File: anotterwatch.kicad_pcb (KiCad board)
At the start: 2 copper layers, 48.5 x 43 mm, 82 parts, among them J1 USB_C_Receptacle_USB2.0, J2 Conn_01x05, Q1 Q_NMOS_GSD, Q2 nfet, Q3 npn, Q4 npn, Q5 2N7002, Q6 2N7002, U1 USBLC6-4SC6, U10 TS5A2053, U11 ADS7946SRTET, U2 ESP32, U3 CH340C, U4 ST7789V, U5 REF2915, U6 TCA9535MRGER, U7 TLV9062S, U8 OPA2322S, U9 TS5A2053

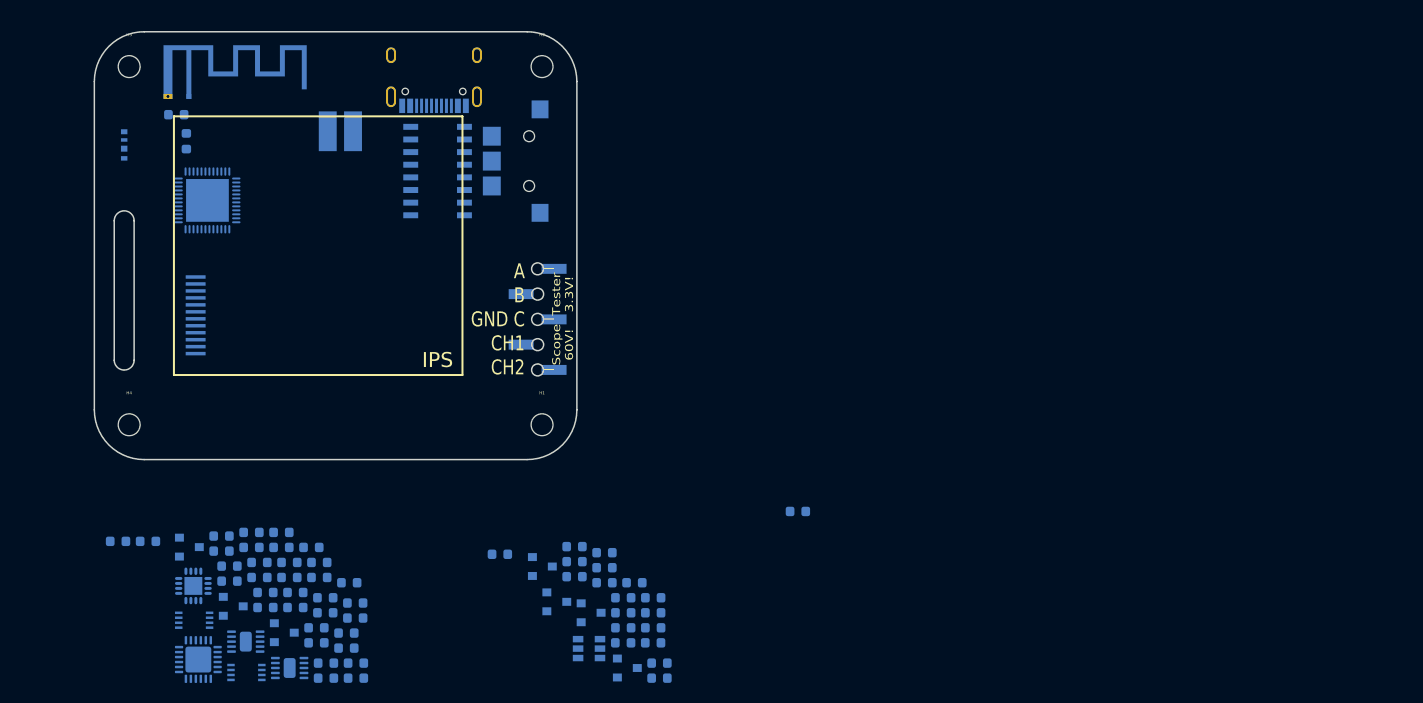
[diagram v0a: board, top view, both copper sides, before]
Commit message: added SD Card socket footprint
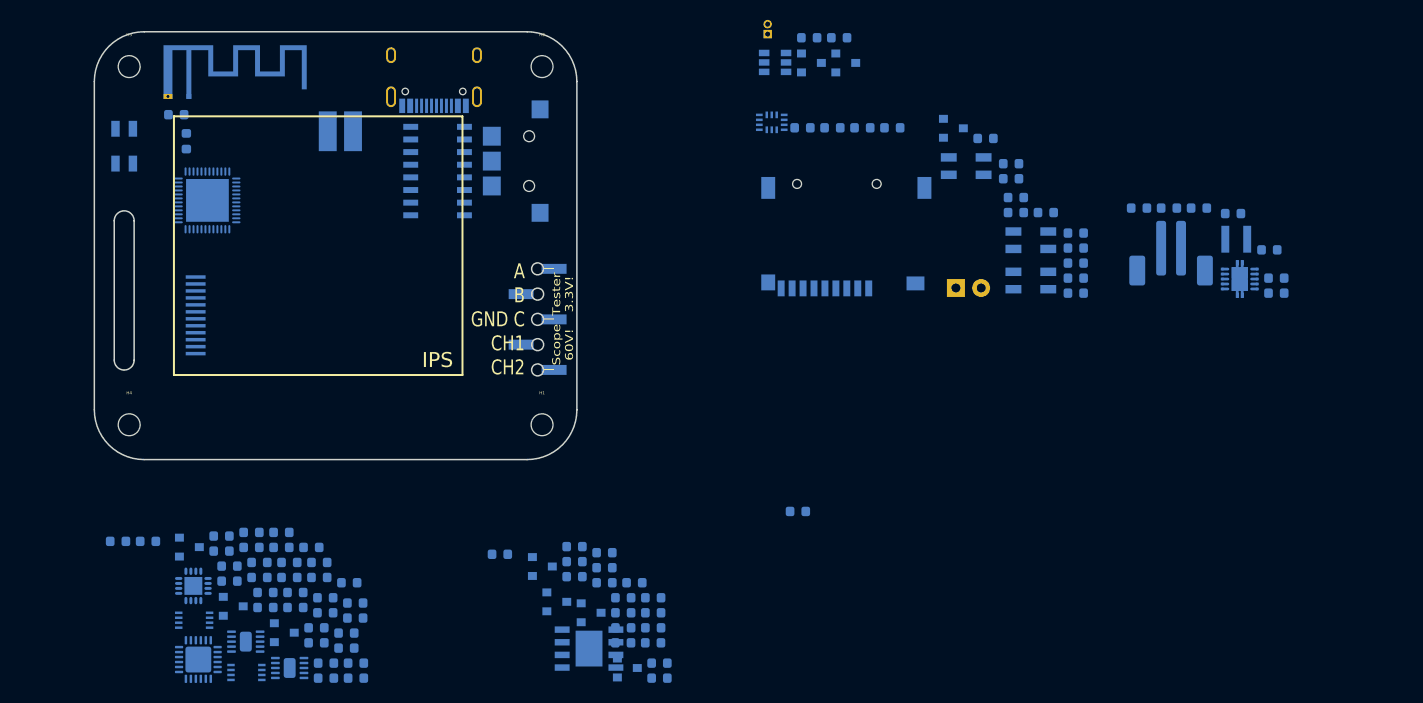
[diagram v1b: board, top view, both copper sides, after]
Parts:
- added C26: 100n, Capacitor_SMD:C_0603_1608Metric, B.Cu at (192.5, 86.8)
- added C27: 100n, Capacitor_SMD:C_0603_1608Metric, B.Cu at (186.0, 86.2)
- added C28: 100n, Capacitor_SMD:C_0603_1608Metric, B.Cu at (189.0, 86.2)
- added C29: 10u, Capacitor_SMD:C_0603_1608Metric, B.Cu at (196.8, 93.3)
- added C30: 100n, Capacitor_SMD:C_0603_1608Metric, B.Cu at (167.6, 79.2)
- added D2: LED, LED_THT:LED_D5.0mm_Horizontal_O1.27mm_Z9.0mm, B.Cu at (164.6, 94.3)
- added D4: SK6812MINI, LED_SMD:LED_SK6812MINI_PLCC4_3.5x3.5mm_P1.75mm, B.Cu at (172.1, 89.5)
- added D5: SK6812MINI, LED_SMD:LED_SK6812MINI_PLCC4_3.5x3.5mm_P1.75mm, B.Cu at (172.1, 93.5)
- added D6: SK6812MINI, LED_SMD:LED_SK6812MINI_PLCC4_3.5x3.5mm_P1.75mm, B.Cu at (165.6, 82.0)
- added FB1: Ferret, Inductor_SMD:L_0603_1608Metric, B.Cu at (152.9, 69.1)
- added J3: Micro_SD_Card, ST-TF-003A:SUNTECH_ST-TF-003A, B.Cu at (152.3, 89.0)
- added J4: Bat, Connector_JST:JST_PH_B2B-PH-SM4-TB_1x02-1MP_P2.00mm_Vertical, B.Cu at (186.2, 90.8)
- added L2: 2.2u, Inductor_SMD:L_Taiyo-Yuden_MD-3030, B.Cu at (192.8, 89.4)
- added LS1: Speaker, Connector_PinHeader_1.00mm:PinHeader_1x02_P1.00mm_Vertical, B.Cu at (145.7, 68.7)
- added Q7: AO3400, Package_TO_SOT_SMD:SOT-23, B.Cu at (164.3, 78.2)
- added Q8: 2N7002, Package_TO_SOT_SMD:SOT-23, B.Cu at (153.5, 71.6)
- added Q9: 2N7002, Package_TO_SOT_SMD:SOT-23, B.Cu at (150.1, 71.6)
- added R30: 10, Resistor_SMD:R_0603_1608Metric, B.Cu at (176.6, 90.2)
- added R31: 47k, Resistor_SMD:R_0603_1608Metric, B.Cu at (173.6, 86.7)
- added R32: 220, Resistor_SMD:R_0603_1608Metric, B.Cu at (170.1, 81.8)
- added R33: 47k, Resistor_SMD:R_0603_1608Metric, B.Cu at (176.6, 88.7)
- added R34: 47k, Resistor_SMD:R_0603_1608Metric, B.Cu at (170.6, 86.7)
- added R35: 10, Resistor_SMD:R_0603_1608Metric, B.Cu at (176.6, 91.8)
- added R36: 47k, Resistor_SMD:R_0603_1608Metric, B.Cu at (196.1, 90.4)
- added R37: 10, Resistor_SMD:R_0603_1608Metric, B.Cu at (170.6, 85.2)
- added R38: 5k1, Resistor_SMD:R_0603_1608Metric, B.Cu at (152.2, 78.2)
- added R39: 5k1, Resistor_SMD:R_0603_1608Metric, B.Cu at (176.6, 94.8)
- added R40: 47k, Resistor_SMD:R_0603_1608Metric, B.Cu at (176.6, 93.3)
- added R41: 47k, Resistor_SMD:R_0603_1608Metric, B.Cu at (158.2, 78.2)
- added R42: 5k1, Resistor_SMD:R_0603_1608Metric, B.Cu at (155.2, 78.2)
- added R43: 2k5, Resistor_SMD:R_0603_1608Metric, B.Cu at (183.0, 86.2)
- added R44: 47k, Resistor_SMD:R_0603_1608Metric, B.Cu at (149.2, 78.2)
- added R45: 47k, Resistor_SMD:R_0603_1608Metric, B.Cu at (170.1, 83.3)
- added R46: 47k, Resistor_SMD:R_0603_1608Metric, B.Cu at (149.9, 69.1)
- added R47: 100, Resistor_SMD:R_0603_1608Metric, B.Cu at (196.8, 94.8)
- added U12: BMI270, badgelib:BMI270, B.Cu at (146.1, 77.6)
- added U13: USBLC6-4SC6, Package_TO_SOT_SMD:SOT-23-6, B.Cu at (146.4, 71.6)
- added U14: TPS63001DRCR, Package_SON:Texas_S-PVSON-N10, B.Cu at (193.1, 93.4)
- C3: value 100n -> 10u
- C6: value 100n -> 4u7
- D1: value SK6812 -> SK6812MINI; footprint badgelib:sk6812_side -> LED_SMD:LED_SK6812MINI_PLCC4_3.5x3.5mm_P1.75mm
- Q1: value Q_NMOS_GSD -> AO3400
- Q2: value nfet -> AO3400
- R10, R9: value 100k -> 47k
- R3, R4, R6: value 10k -> 47k
- U1: value USBLC6-4SC6 -> TP4056; footprint Package_TO_SOT_SMD:SOT-23-6 -> Package_SO:Diodes_PSOP-8
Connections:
- net CH340_V3 renamed Net-(C4-Pad1)
- net Net-(U2-Pad5) renamed ESP_ADC
- C10 pad 1: VCC -> TPS_FB
- C13 pad 1: +3V3 -> TPS_FB
- C14 pad 1: +3V3 -> TPS_FB
- C15 pad 1: +3V3 -> TPS_FB
- C17 pad 1: +3V3 -> TPS_FB
- C19 pad 1: +3V3 -> TPS_FB
- C2 pad 1: VCC -> VBUS
- C24 pad 2: GNDA -> Net-(C24-Pad2)
- C25 pad 2: GNDA -> Net-(C25-Pad2)
- C3 pad 1: VCC -> +BATT
- C5 pad 1: VBUS -> IPS_RST
- C6 pad 1: VCC -> Net-(C6-Pad1)
- C6 pad 2: GND -> Net-(C6-Pad2)
- C7 pad 1: VCC -> Net-(C7-Pad1)
- C7 pad 2: GND -> GNDA
- C8 pad 1: VCC -> TPS_FB
- J1 pad A6: Dp -> USB_DP
- J1 pad A7: Dn -> USB_DN
- J1 pad B6: Dp -> USB_DP
- J1 pad B7: Dn -> USB_DN
- Q1 pad 1: White_LED -> WHITE_LED
- Q5 pad 3: Net-(Q5-Pad3) -> Net-(C24-Pad2)
- Q6 pad 3: Net-(Q6-Pad3) -> Net-(C25-Pad2)
- R10 pad 2: Net-(R10-Pad2) -> ESP32_DAC
- R12 pad 2: Net-(R12-Pad2) -> Net-(C6-Pad1)
- R28 pad 1: Net-(Q5-Pad3) -> Net-(C24-Pad2)
- R29 pad 1: Net-(Q6-Pad3) -> Net-(C25-Pad2)
- R3 pad 1: VCC -> TPS_FB
- R4 pad 1: White_LED -> WHITE_LED
- R6 pad 1: IPS_LED -> TPS_FB
- R6 pad 2: GND -> IO0
- R9 pad 1: Net-(R10-Pad2) -> ESP32_DAC
- S1 pad 1: Net-(S1-Pad1) -> BTN_UP
- S1 pad 2: Net-(S1-Pad2) -> BTN_DOWN
- S1 pad T: Net-(S1-PadT) -> BTN_CNTR
- U1 pad 1: Net-(U1-Pad1) -> GND
- U1 pad 2: GND -> Net-(R43-Pad1)
- U1 pad 3: Net-(U1-Pad3) -> GND
- U1 pad 4: Dp -> VBUS
- U1 pad 5: VCC -> +BATT
- U1 pad 6: Dn -> Net-(U1-Pad6)
- U10 pad 8: +3V3 -> TPS_FB
- U11 pad 11: Net-(U11-Pad11) -> ADC_CH_SEL
- U11 pad 12: Net-(U11-Pad12) -> ADC_ENABLE
- U11 pad 13: Net-(U11-Pad13) -> ADC_CS
- U11 pad 14: Net-(U11-Pad14) -> ADC_SCK
- U11 pad 15: Net-(U11-Pad15) -> ADC_MISO
- U11 pad 16: Net-(U11-Pad16) -> TPS_FB
- U11 pad 17: Net-(U11-Pad17) -> GND
- U11 pad 2: Net-(U11-Pad2) -> Net-(C7-Pad1)
- U2 pad 1: VCC -> TPS_FB
- U2 pad 10: Net-(U2-Pad10) -> BTN_CNTR
- U2 pad 11: Net-(U2-Pad11) -> WAKE1
- U2 pad 12: Net-(U2-Pad12) -> WHITE_LED
- U2 pad 13: Net-(U2-Pad13) -> IPS_LED
- U2 pad 14: Net-(U2-Pad14) -> ESP32_DAC
- U2 pad 15: Net-(U2-Pad15) -> IPS_DC
- U2 pad 16: Net-(U2-Pad16) -> ADC_CH_SEL
- U2 pad 17: Net-(U2-Pad17) -> SD_CLK
- U2 pad 18: Net-(U2-Pad18) -> SD_DATA2
- U2 pad 19: VCC -> TPS_FB
- U2 pad 20: Net-(U2-Pad20) -> SD_DATA3
- U2 pad 21: Net-(U2-Pad21) -> SD_CMD
- U2 pad 22: Net-(U2-Pad22) -> SD_DATA0
- U2 pad 24: Net-(U2-Pad24) -> SD_DATA1
- U2 pad 3: VCC -> TPS_FB
- U2 pad 34: Net-(U2-Pad34) -> ADC_CS
- U2 pad 36: Net-(U2-Pad36) -> IPS_MOSI
- U2 pad 37: VCC -> TPS_FB
- U2 pad 38: Net-(U2-Pad38) -> ADC_MISO
- U2 pad 39: Net-(U2-Pad39) -> I2C_SCL
- U2 pad 4: VCC -> TPS_FB
- U2 pad 42: Net-(U2-Pad42) -> I2C_SDA
- U2 pad 43: VCC -> TPS_FB
- U2 pad 46: VCC -> TPS_FB
- U2 pad 6: Net-(U2-Pad6) -> CHRG
- U2 pad 7: Net-(U2-Pad7) -> BTN_UP
- U2 pad 8: Net-(U2-Pad8) -> BTN_DOWN
- U3 pad 5: Dp -> USB_DP
- U3 pad 6: Dn -> USB_DN
- U4 pad 3: VCC -> TPS_FB
- U4 pad 4: VCC -> TPS_FB
- U4 pad 7: IPS_CD -> IPS_DC
- U4 pad 8: IPS_CS -> GND
- U4 pad 9: VCC -> ADC_SCK
- U6 pad 19: SCL -> I2C_SCL
- U6 pad 20: SDA -> I2C_SDA
- U6 pad 21: +3V3 -> TPS_FB
- U6 pad 7: Net-(U6-Pad7) -> PARTY_ENABLE
- U7 pad 1: Net-(R12-Pad2) -> Net-(C6-Pad1)
- U7 pad 10: +3V3 -> TPS_FB
- U7 pad 2: Net-(R12-Pad2) -> Net-(C6-Pad1)
- U7 pad 3: Net-(R10-Pad2) -> ESP32_DAC
- U8 pad 10: +3V3 -> TPS_FB
- U9 pad 8: +3V3 -> TPS_FB

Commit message: UPD: finalized schematic, started layout
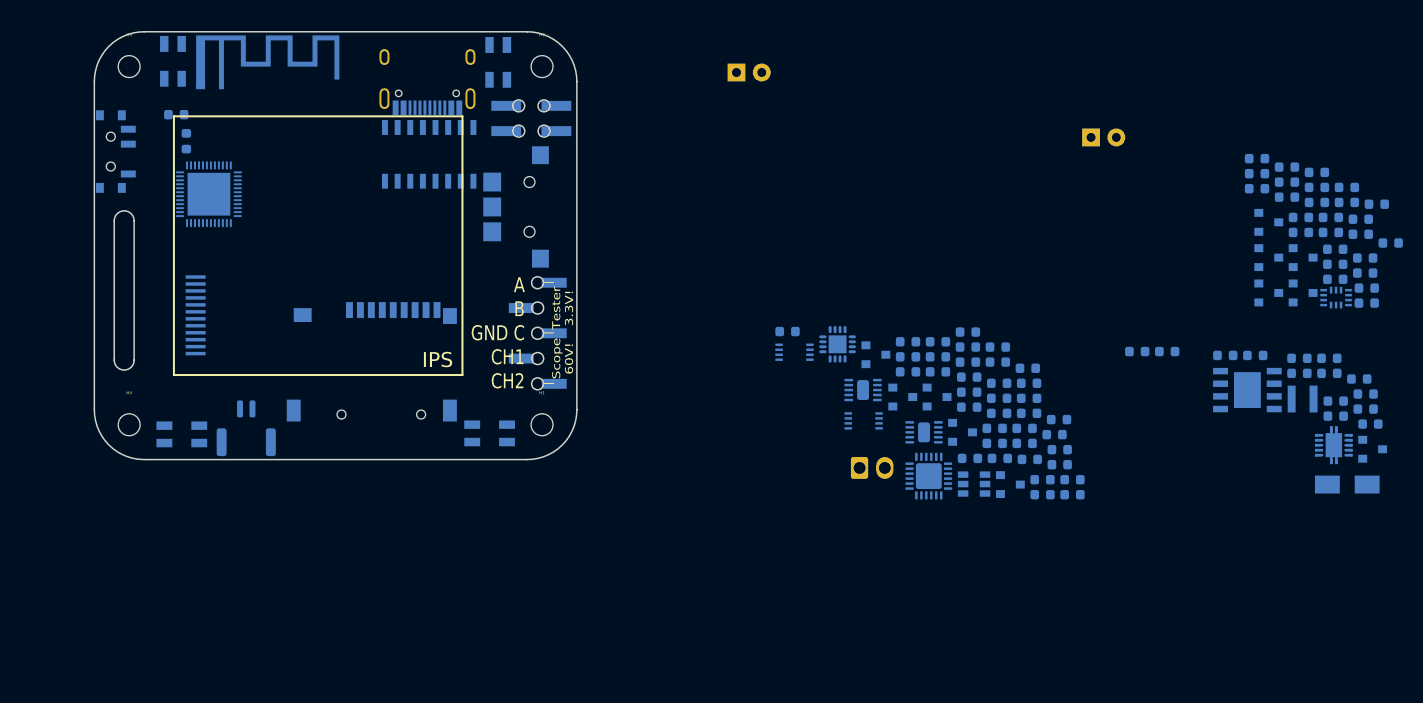
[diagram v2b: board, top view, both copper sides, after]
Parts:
- added BT1: 603020, Connector_JST:JST_GH_BM02B-GHS-TBT_1x02-1MP_P1.25mm_Vertical, B.Cu at (93.3, 108.4)
- added D7: D_Small, Diode_SMD:D_SMA, B.Cu at (203.9, 114.0)
- added Q10: Q_PMOS_GDS, Package_TO_SOT_SMD:SOT-23, B.Cu at (206.5, 110.5)
- added SW1: SW_SPST, Button_Switch_SMD:SW_SPDT_PCM12, B.Cu at (80.0, 80.5)
- C1: value 100p -> 100n
- C11, C12: value TBD -> 100n
- C15: value 100n -> 4u7
- C17, C18: value 100n -> 6n8
- C19: value 100n -> 1n
- C20: value 6n8 -> 1n
- C21: value 6n8 -> 33p
- C22: value 1n -> 33p
- C23: value 1n -> 100n
- C24: value 33p -> 100p
- C25: value 33p -> 10u
- C26, C27, C30: value 100n -> 10u
- C29, C8: value 10u -> 100n
- C6: value 4u7 -> TBD
- C7: value 100n -> TBD
- D2, D3: value LED -> SK6812MINI; footprint LED_THT:LED_D5.0mm_Horizontal_O1.27mm_Z9.0mm -> LED_SMD:LED_SK6812MINI_PLCC4_3.5x3.5mm_P1.75mm
- D5, D6: value SK6812MINI -> LED; footprint LED_SMD:LED_SK6812MINI_PLCC4_3.5x3.5mm_P1.75mm -> LED_THT:LED_D5.0mm_Horizontal_O1.27mm_Z9.0mm
- J1: value USB_C_Receptacle_USB2.0 -> Conn_02x02_Odd_Even; footprint badgelib:USB-C 16Pin -> Connector_PinSocket_2.54mm:PinSocket_2x02_P2.54mm_Vertical_SMD
- J2: value Conn_01x05 -> Micro_SD_Card; footprint Connector_PinHeader_2.54mm:PinHeader_1x05_P2.54mm_Vertical_SMD_Pin1Left -> ST-TF-003A:SUNTECH_ST-TF-003A
- J3: value Micro_SD_Card -> Conn_01x05; footprint ST-TF-003A:SUNTECH_ST-TF-003A -> Connector_PinHeader_2.54mm:PinHeader_1x05_P2.54mm_Vertical_SMD_Pin1Left
- J4: value Bat -> USB_C_Receptacle_USB2.0; footprint Connector_JST:JST_PH_B2B-PH-SM4-TB_1x02-1MP_P2.00mm_Vertical -> badgelib:USB-C 16Pin
- LS1: footprint Connector_PinHeader_1.00mm:PinHeader_1x02_P1.00mm_Vertical -> Connector_Molex:Molex_KK-254_AE-6410-02A_1x02_P2.54mm_Vertical
- Q3, Q4: value npn -> AO3400
- Q5: value 2N7002 -> AO3400
- Q7: value AO3400 -> 2N7002
- R11, R18: value 680 -> 10
- R13, R15: value 390k -> 10
- R14: value 680 -> 47k
- R16, R17: value 390k -> 47k
- R19, R20: value 10M -> 47k
- R21, R28: value 10M -> 680
- R22: value 10M -> 100
- R24: value 390k -> 680
- R26, R27: value 2M2 -> 390k
- R30: value 10 -> 10M
- R31, R40: value 47k -> 10M
- R32: value 220 -> 10M
- R33, R34: value 47k -> 390k
- R35: value 10 -> 390k
- R37: value 10 -> 2M2
- R38: value 5k1 -> 2M2
- R39: value 5k1 -> 10M
- R41, R44, R45, R9: value 47k -> 5k1
- R43: value 2k5 -> 390k
- R5: value 10 -> 47k
- R7, R8: value 10k -> 47k
- U1: value TP4056 -> BMI270; footprint Package_SO:Diodes_PSOP-8 -> badgelib:BMI270
- U11: value ADS7946SRTET -> TS5A2053; footprint Package_DFN_QFN:QFN-16-1EP_3x3mm_P0.5mm_EP1.8x1.8mm -> Package_SO:VSSOP-8_2.4x2.1mm_P0.5mm
- U12: value BMI270 -> ADS7946SRTET; footprint badgelib:BMI270 -> Package_DFN_QFN:QFN-16-1EP_3x3mm_P0.5mm_EP1.8x1.8mm
- U13: value USBLC6-4SC6 -> TP4056; footprint Package_TO_SOT_SMD:SOT-23-6 -> Package_SO:Diodes_PSOP-8
- U2: value ESP32 -> CH340C; footprint ESP32-footprints-Lib:ESP32 -> Package_SO:SOIC-16_3.9x9.9mm_P1.27mm
- U3: value CH340C -> ESP32; footprint Package_SO:SOIC-16_3.9x9.9mm_P1.27mm -> ESP32-footprints-Lib:ESP32
- U9: value TS5A2053 -> USBLC6-4SC6; footprint Package_SO:VSSOP-8_2.4x2.1mm_P0.5mm -> Package_TO_SOT_SMD:SOT-23-6
- moved R15 121.2 mm to (208.3, 89.7)
- moved R12 120.3 mm to (194.9, 82.8)
- moved R11 120.0 mm to (197.9, 83.6)
- moved R14 119.1 mm to (203.9, 84.1)
- moved R17 116.8 mm to (205.3, 87.3)
- moved R16 111.1 mm to (200.9, 82.6)
- moved Q5 111.0 mm to (196.0, 87.7)
- moved R13 110.5 mm to (202.3, 88.7)
- moved R10 109.8 mm to (205.7, 91.2)
- moved R18 107.5 mm to (203.9, 85.7)
- moved R9 104.5 mm to (200.9, 85.7)
- moved C24 103.6 mm to (199.1, 102.8)
- moved C25 103.0 mm to (202.1, 101.3)
- moved C8 88.4 mm to (202.7, 93.4)
- moved D4 87.5 mm to (86.8, 109.0), turned to 180 degrees
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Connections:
- C1 pad 1: Net-(C1-Pad1) -> VBUS
- C10 pad 1: TPS_FB -> +3V3
- C11 pad 1: Net-(C11-Pad1) -> +3V3
- C12 pad 1: Net-(AE1-Pad1) -> AFE_ENABLE
- C12 pad 2: GND -> GNDA
- C13 pad 1: TPS_FB -> +3V3
- C14 pad 1: TPS_FB -> ADC_REF
- C14 pad 2: GND -> GNDA
- C15 pad 1: TPS_FB -> Net-(C15-Pad1)
- C15 pad 2: GND -> Net-(C15-Pad2)
- C16 pad 1: AFE_ENABLE -> +3V3
- C16 pad 2: GNDA -> GND
- C17 pad 1: TPS_FB -> Net-(C17-Pad1)
- C17 pad 2: GND -> GNDA
- C18 pad 1: ADC_REF -> Net-(C18-Pad1)
- C19 pad 1: TPS_FB -> Net-(C19-Pad1)
- C19 pad 2: GND -> PROBE1
- C2 pad 1: VBUS -> Net-(C2-Pad1)
- C20 pad 2: GNDA -> PROBE2
- C21 pad 1: Net-(C21-Pad1) -> PROBE1
- C21 pad 2: GNDA -> Net-(C21-Pad2)
- C22 pad 1: Net-(C22-Pad1) -> PROBE2
- C22 pad 2: PROBE1 -> Net-(C22-Pad2)
- C23 pad 2: PROBE2 -> GNDA
- C24 pad 1: PROBE1 -> GND
- C25 pad 1: PROBE2 -> VBUS
- C25 pad 2: Net-(C25-Pad2) -> GND
- C26 pad 1: Net-(C26-Pad1) -> Net-(BT1-Pad1)
- C28 pad 1: TPS_FB -> Net-(C28-Pad1)
- C29 pad 1: TPS_FB -> +3V3
- C3 pad 1: +BATT -> +3V3
- C30 pad 1: VBUS -> +3V3
- C4 pad 1: Net-(C4-Pad1) -> EN
- C5 pad 1: IPS_RST -> +3V3
- C6 pad 2: Net-(C6-Pad2) -> GND
- C7 pad 1: Net-(C7-Pad1) -> Net-(AE1-Pad1)
- C7 pad 2: GNDA -> GND
- C8 pad 1: TPS_FB -> IPS_RST
- C9 pad 1: EN -> +3V3
- D1 pad 4: TPS_FB -> +3V3
- D2 pad 2: Net-(D2-Pad2) -> Net-(D1-Pad2)
- D3 pad 1: Net-(D2-Pad1) -> Net-(D3-Pad1)
- D3 pad 2: Net-(D3-Pad2) -> Net-(D1-Pad2)
- D4 pad 3: Net-(D1-Pad1) -> Net-(D3-Pad1)
- D4 pad 4: TPS_FB -> +3V3
- D5 pad 2: Net-(D1-Pad2) -> Net-(D5-Pad2)
- D6 pad 1: Net-(D6-Pad1) -> Net-(D5-Pad1)
- D6 pad 2: Net-(D1-Pad2) -> Net-(D6-Pad2)
- FB1 pad 1: Net-(C7-Pad1) -> Net-(C23-Pad1)
- FB1 pad 2: TPS_FB -> +3V3
- J2 pad 1: Net-(J2-Pad1) -> SD_DATA2
- J2 pad 2: Net-(J2-Pad2) -> SD_DATA3
- J2 pad 3: Net-(J2-Pad3) -> SD_CMD
- J2 pad 4: Net-(J2-Pad4) -> +3V3
- J3 pad 1: SD_DATA2 -> Net-(J3-Pad1)
- J3 pad 2: SD_DATA3 -> Net-(J3-Pad2)
- J3 pad 3: SD_CMD -> Net-(J3-Pad3)
- J3 pad 4: TPS_FB -> Net-(J3-Pad4)
- L1 pad 1: Net-(C11-Pad1) -> Net-(C6-Pad1)
- LS1 pad 1: Net-(C6-Pad2) -> Net-(C15-Pad2)
- Q1 pad 1: WHITE_LED -> DTR
- Q1 pad 2: GND -> RTS
- Q1 pad 3: Net-(D2-Pad1) -> EN
- Q2 pad 1: IPS_LED -> RTS
- Q2 pad 2: GND -> DTR
- Q2 pad 3: Net-(Q2-Pad3) -> IO0
- Q3 pad 1: Net-(Q3-Pad1) -> PARTY_ENABLE
- Q3 pad 2: Net-(Q3-Pad2) -> GND
- Q3 pad 3: EN -> Net-(D1-Pad2)
- Q4 pad 1: Net-(Q3-Pad2) -> IPS_LED
- Q4 pad 2: Net-(Q3-Pad1) -> GND
- Q4 pad 3: IO0 -> Net-(Q4-Pad3)
- Q5 pad 1: SE_ENABLE -> WHITE_LED
- Q5 pad 2: GNDA -> GND
- Q5 pad 3: Net-(C24-Pad2) -> Net-(D5-Pad1)
- Q6 pad 1: SE_ENABLE -> BUF_ENABLE
- Q6 pad 2: GNDA -> GND
- Q6 pad 3: Net-(C25-Pad2) -> Net-(LS1-Pad2)
- Q7 pad 1: PARTY_ENABLE -> AFE_ENABLE
- Q7 pad 3: Net-(D1-Pad2) -> ADC_ENABLE
- Q8 pad 1: AFE_ENABLE -> SE_ENABLE
- Q8 pad 2: GND -> GNDA
- Q8 pad 3: ADC_ENABLE -> Net-(C21-Pad2)
- Q9 pad 1: BUF_ENABLE -> SE_ENABLE
- Q9 pad 2: GND -> GNDA
- Q9 pad 3: Net-(LS1-Pad2) -> Net-(C22-Pad2)
- R1 pad 1: GND -> I2C_SDA
- R1 pad 2: Net-(J1-PadA5) -> +3V3
- R10 pad 1: GNDA -> +3V3
- R10 pad 2: ESP32_DAC -> BTN_CNTR
- R11 pad 1: Net-(J2-Pad3) -> Net-(J2-Pad5)
- R11 pad 2: Net-(R11-Pad2) -> SD_CLK
- R12 pad 1: Net-(J2-Pad3) -> Net-(J2-Pad7)
- R12 pad 2: Net-(C6-Pad1) -> SD_DATA0
- R13 pad 1: Net-(J2-Pad3) -> ADC_SCK
- R14 pad 1: Net-(J2-Pad2) -> PARTY_ENABLE
- R14 pad 2: Net-(R14-Pad2) -> GND
- R15 pad 1: Net-(J2-Pad2) -> +BATT
- R15 pad 2: Net-(R15-Pad2) -> Net-(D5-Pad2)
- R16 pad 1: Net-(C20-Pad1) -> WHITE_LED
- R16 pad 2: ADC_REF -> GND
- R17 pad 1: Net-(C21-Pad1) -> +3V3
- R17 pad 2: ADC_REF -> IPS_RST
- R18 pad 1: Net-(J2-Pad1) -> +BATT
- R18 pad 2: Net-(R18-Pad2) -> Net-(D6-Pad2)
- R19 pad 1: Net-(J2-Pad1) -> ESP32_DAC
- R19 pad 2: PROBE1 -> ADC_REF
- R2 pad 1: GND -> +3V3
- R2 pad 2: Net-(J1-PadB5) -> I2C_SCL
- R20 pad 1: Net-(J2-Pad2) -> GNDA
- R20 pad 2: PROBE2 -> ESP32_DAC
- R21 pad 1: Net-(J2-Pad4) -> Net-(J3-Pad3)
- R21 pad 2: PROBE1 -> Net-(R21-Pad2)
- R22 pad 1: Net-(J2-Pad5) -> Net-(J3-Pad3)
- R22 pad 2: PROBE2 -> Net-(C15-Pad1)
- R23 pad 1: GNDA -> Net-(J3-Pad3)
- R23 pad 2: Net-(C20-Pad1) -> Net-(R23-Pad2)
- R24 pad 1: GNDA -> Net-(J3-Pad2)
- R24 pad 2: Net-(C21-Pad1) -> Net-(R24-Pad2)
- R25 pad 1: Net-(J2-Pad1) -> Net-(J3-Pad2)
- R26 pad 1: PROBE1 -> Net-(C17-Pad1)
- R26 pad 2: Net-(C22-Pad1) -> ADC_REF
- R27 pad 1: PROBE2 -> Net-(C18-Pad1)
- R27 pad 2: Net-(C23-Pad1) -> ADC_REF
- R28 pad 1: Net-(C24-Pad2) -> Net-(J3-Pad1)
- R28 pad 2: PROBE1 -> Net-(R28-Pad2)
- R29 pad 1: Net-(C25-Pad2) -> Net-(J3-Pad1)
- R29 pad 2: PROBE2 -> PROBE1
- R3 pad 1: TPS_FB -> +3V3
- R3 pad 2: EN -> SD_DATA0
- R30 pad 1: Net-(J3-Pad5) -> Net-(J3-Pad2)
- R30 pad 2: SD_CLK -> PROBE2
- R31 pad 1: TPS_FB -> Net-(J3-Pad4)
- R31 pad 2: BTN_UP -> PROBE1
- R32 pad 1: Net-(J3-Pad7) -> Net-(J3-Pad5)
- R32 pad 2: SD_DATA0 -> PROBE2
- R33 pad 1: TPS_FB -> GNDA
- R33 pad 2: BTN_DOWN -> Net-(C17-Pad1)
- R34 pad 1: TPS_FB -> GNDA
- R34 pad 2: BTN_CNTR -> Net-(C18-Pad1)
- R35 pad 1: ADC_SCK -> Net-(J3-Pad1)
- R36 pad 1: TPS_FB -> ADC_ENABLE
- R36 pad 2: CHRG -> +3V3
- R37 pad 1: +BATT -> PROBE1
- R37 pad 2: Net-(D2-Pad2) -> Net-(C19-Pad1)
- R38 pad 1: I2C_SDA -> PROBE2
- R38 pad 2: TPS_FB -> Net-(C20-Pad1)
- R39 pad 1: TPS_FB -> Net-(C21-Pad2)
- R39 pad 2: I2C_SCL -> PROBE1
- R4 pad 1: WHITE_LED -> +3V3
- R4 pad 2: GND -> IO0
- R40 pad 1: TPS_FB -> Net-(C22-Pad2)
- R40 pad 2: SD_DATA0 -> PROBE2
- R41 pad 1: TPS_FB -> GND
- R41 pad 2: SD_DATA3 -> Net-(J4-PadA5)
- R42 pad 1: TPS_FB -> GND
- R42 pad 2: SD_CMD -> Net-(J4-PadB5)
- R43 pad 1: Net-(R43-Pad1) -> +3V3
- R43 pad 2: GND -> CHRG
- R44 pad 1: PARTY_ENABLE -> Net-(R44-Pad1)
- R45 pad 1: TPS_FB -> Net-(R44-Pad1)
- R45 pad 2: IPS_RST -> GND
- R46 pad 1: ADC_ENABLE -> VBUS
- R46 pad 2: TPS_FB -> GND
- R47 pad 2: Net-(C26-Pad1) -> Net-(C28-Pad1)
- R5 pad 1: +BATT -> +3V3
- R5 pad 2: Net-(D3-Pad2) -> BTN_UP
- R6 pad 1: TPS_FB -> +3V3
- R6 pad 2: IO0 -> SD_DATA3
- R7 pad 1: DTR -> +3V3
- R7 pad 2: Net-(Q3-Pad1) -> EN
- R8 pad 1: Net-(Q3-Pad2) -> +3V3
- R8 pad 2: RTS -> BTN_DOWN
- R9 pad 1: ESP32_DAC -> +3V3
- R9 pad 2: ADC_REF -> SD_CMD
- U1 pad 2: Net-(R43-Pad1) -> Net-(U1-Pad2)
- U1 pad 3: GND -> Net-(U1-Pad3)
- U1 pad 4: VBUS -> WAKE1
- U1 pad 5: +BATT -> +3V3
- U1 pad 6: Net-(U1-Pad6) -> GND
- U1 pad 7: CHRG -> GND
- U1 pad 8: VBUS -> +3V3
- U1 pad 9: (no net) -> Net-(U1-Pad9)
- U10 pad 1: Net-(C21-Pad1) -> Net-(C17-Pad1)
- U10 pad 5: MUX_CH2 -> MUX_CH1
- U10 pad 6: PROBE2 -> PROBE1
- U10 pad 7: Net-(C23-Pad1) -> Net-(C19-Pad1)
- U10 pad 8: TPS_FB -> +3V3
- U11 pad 1: GND -> Net-(C18-Pad1)
- U11 pad 2: Net-(C7-Pad1) -> MUX_ENABLE
- U11 pad 3: ADC_REF -> GND
- U11 pad 4: GNDA -> GND
- U11 pad 5: Net-(U11-Pad5) -> MUX_CH2
- U11 pad 6: GNDA -> PROBE2
- U11 pad 7: GNDA -> Net-(C20-Pad1)
- U11 pad 8: Net-(U11-Pad8) -> +3V3
- U12 pad 11: Net-(U12-Pad11) -> ADC_CH_SEL
- U12 pad 12: TPS_FB -> ADC_ENABLE
- U12 pad 13: I2C_SCL -> ADC_CS
- U12 pad 14: I2C_SDA -> ADC_SCK
- U12 pad 2: Net-(U12-Pad2) -> Net-(C23-Pad1)
- U12 pad 3: Net-(U12-Pad3) -> ADC_REF
- U12 pad 4: WAKE1 -> GNDA
- U12 pad 5: TPS_FB -> Net-(U12-Pad5)
- U12 pad 6: GND -> GNDA
- U12 pad 7: GND -> GNDA
- U12 pad 8: TPS_FB -> Net-(U12-Pad8)
- U13 pad 1: Net-(J2-Pad2) -> GND
- U13 pad 2: GND -> Net-(R44-Pad1)
- U13 pad 3: PROBE2 -> GND
- U13 pad 4: PROBE1 -> VBUS
- U13 pad 5: TPS_FB -> Net-(BT1-Pad1)
- U13 pad 6: Net-(J2-Pad1) -> Net-(U13-Pad6)
- U14 pad 1: TPS_FB -> +3V3
- U14 pad 10: TPS_FB -> +3V3
- U14 pad 6: Net-(C26-Pad1) -> Net-(C28-Pad1)
- U14 pad 7: Net-(C26-Pad1) -> Net-(C28-Pad1)
- U14 pad 8: Net-(C26-Pad1) -> Net-(C28-Pad1)
- U2 pad 1: TPS_FB -> GND
- U2 pad 10: BTN_CNTR -> Net-(U2-Pad10)
- U2 pad 11: WAKE1 -> Net-(U2-Pad11)
- U2 pad 12: WHITE_LED -> Net-(U2-Pad12)
- U2 pad 13: IPS_LED -> DTR
- U2 pad 14: ESP32_DAC -> RTS
- U2 pad 15: IPS_DC -> Net-(U2-Pad15)
- U2 pad 16: ADC_CH_SEL -> VBUS
- U2 pad 2: Net-(C11-Pad1) -> TXD
- U2 pad 3: TPS_FB -> RXD
- U2 pad 4: TPS_FB -> Net-(C2-Pad1)
- U2 pad 5: ESP_ADC -> USB_DP
- U2 pad 6: CHRG -> USB_DN
- U2 pad 7: BTN_UP -> Net-(U2-Pad7)
- U2 pad 8: BTN_DOWN -> Net-(U2-Pad8)
- U2 pad 9: EN -> Net-(U2-Pad9)
- U3 pad 1: GND -> +3V3
- U3 pad 10: Net-(U3-Pad10) -> BTN_CNTR
- U3 pad 11: Net-(U3-Pad11) -> WAKE1
- U3 pad 12: Net-(U3-Pad12) -> WHITE_LED
- U3 pad 13: DTR -> IPS_LED
- U3 pad 14: RTS -> ESP32_DAC
- U3 pad 15: Net-(U3-Pad15) -> IPS_DC
- U3 pad 16: VBUS -> ADC_CH_SEL
- U3 pad 2: TXD -> Net-(C6-Pad1)
- U3 pad 3: RXD -> +3V3
- U3 pad 4: Net-(C4-Pad1) -> +3V3
- U3 pad 5: USB_DP -> ESP_ADC
- U3 pad 6: USB_DN -> CHRG
- U3 pad 7: Net-(U3-Pad7) -> BTN_UP
- U3 pad 8: Net-(U3-Pad8) -> BTN_DOWN
- U3 pad 9: Net-(U3-Pad9) -> EN
- U4 pad 2: Net-(Q2-Pad3) -> Net-(Q4-Pad3)
- U4 pad 3: TPS_FB -> +3V3
- U4 pad 4: TPS_FB -> +3V3
- U4 pad 9: ADC_SCK -> +3V3
- U6 pad 10: Net-(R18-Pad2) -> Net-(R28-Pad2)
- U6 pad 11: Net-(J2-Pad1) -> Net-(J3-Pad1)
- U6 pad 12: Net-(R15-Pad2) -> Net-(R25-Pad2)
- U6 pad 13: Net-(R14-Pad2) -> Net-(R24-Pad2)
- U6 pad 14: Net-(J2-Pad2) -> Net-(J3-Pad2)
- U6 pad 15: Net-(R13-Pad2) -> Net-(R23-Pad2)
- U6 pad 16: Net-(R11-Pad2) -> Net-(R21-Pad2)
- U6 pad 17: Net-(J2-Pad3) -> Net-(J3-Pad3)
- U6 pad 21: TPS_FB -> +3V3
- U6 pad 8: Net-(R25-Pad2) -> Net-(R35-Pad2)
- U7 pad 1: Net-(C6-Pad1) -> Net-(C15-Pad1)
- U7 pad 10: TPS_FB -> +3V3
- U7 pad 2: Net-(C6-Pad1) -> Net-(C15-Pad1)
- U7 pad 7: Net-(J2-Pad3) -> Net-(J3-Pad3)
- U8 pad 1: Net-(U11-Pad5) -> Net-(U12-Pad5)
- U8 pad 10: TPS_FB -> +3V3
- U8 pad 2: Net-(U11-Pad5) -> Net-(U12-Pad5)
- U8 pad 8: Net-(U11-Pad8) -> Net-(U12-Pad8)
- U8 pad 9: Net-(U11-Pad8) -> Net-(U12-Pad8)
- U9 pad 1: Net-(C20-Pad1) -> Net-(J3-Pad2)
- U9 pad 2: MUX_ENABLE -> GND
- U9 pad 3: GND -> PROBE2
- U9 pad 4: GND -> PROBE1
- U9 pad 5: MUX_CH1 -> +3V3
- U9 pad 6: PROBE1 -> Net-(J3-Pad1)
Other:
- outline, holes or cut-outs redrawn

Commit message: Finalized front
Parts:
- removed D5, D6: LED, LED_THT:LED_D5.0mm_Horizontal_O1.27mm_Z9.0mm
- removed LS1: Speaker, Connector_Molex:Molex_KK-254_AE-6410-02A_1x02_P2.54mm_Vertical
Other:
- outline, holes or cut-outs redrawn
